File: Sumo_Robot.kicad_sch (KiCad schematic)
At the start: 0 parts

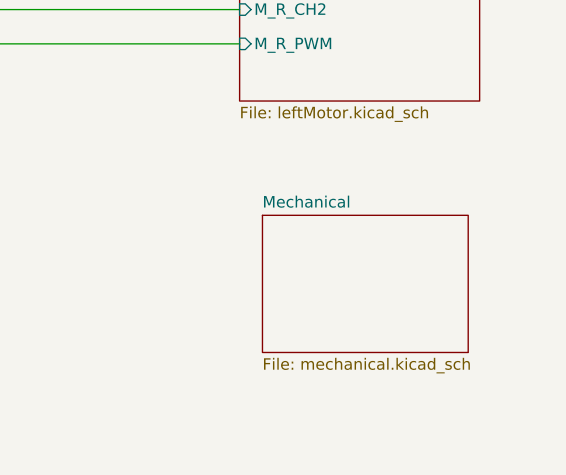
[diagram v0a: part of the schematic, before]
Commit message: removed mechanical sheet
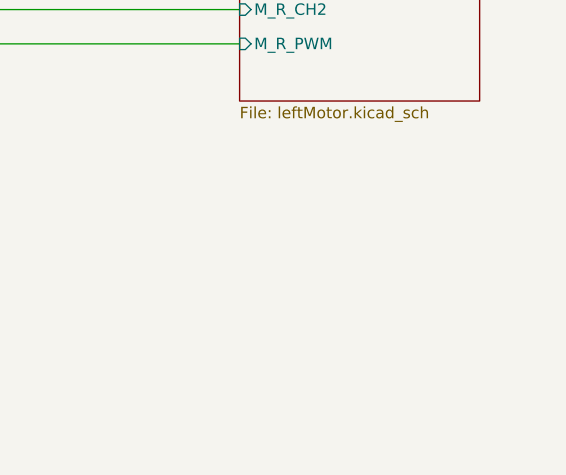
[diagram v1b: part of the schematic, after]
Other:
- removed sheet Mechanical
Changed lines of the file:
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@@
-	)
-	(sheet
-		(at 233.68 111.76)
-		(size 22.86 15.24)
-		(exclude_from_sim no)
-		(in_bom yes)
-		(on_board yes)
-		(dnp no)
-		(fields_autoplaced yes)
-		(stroke
-			(width 0.1524)
-			(type solid)
-			(color 0 0 0 1)
-		)
-		(fill
-			(color 148 255 23 1.0000)
-		)
-		(property "Sheetname" "Mechanical"
-			(at 233.68 111.0484 0)
-			(effects
-				(font
-					(size 1.27 1.27)
-				)
-				(justify left bottom)
-			)
-		)
-		(property "Sheetfile" "mechanical.kicad_sch"
-			(at 233.68 127.5846 0)
-			(effects
-				(font
-					(size 1.27 1.27)
-				)
-				(justify left top)
-			)
-		)
-		(instances
-			(project "Sumo_Robot"
-				(path "/f283bc71-7763-4093-b75c-cbe2f5868c12"
-					(page "10")
-				)
-			)
-		)
 	)
 	(sheet

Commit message: updated infomration on schematic; started working on layout
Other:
- company: (none) -> Erick Zamora 
- title: (none) -> Miniature Sumo Robot 
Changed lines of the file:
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@@
 	(generator_version "9.0")
 	(paper "A4")
+	(title_block
+		(title "Miniature Sumo Robot ")
+		(date "2025-09-26")
+		(rev "A")
+		(company "Erick Zamora ")
+	)
 	(wire
 		(pts
